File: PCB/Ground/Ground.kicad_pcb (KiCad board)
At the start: 2 copper layers, 100 x 86.6 mm, 40 parts, among them J1 Conn_01x05_Female, U1 HT16K33-28SOP

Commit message: [update] Groundのネットリストを作成 #4
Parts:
- removed D10, D11, D12, D13, D14, D15, D16, D17, D18, D19, D20, D21, D22, D23, D24, D4, D5, D6, D7, D8, D9: LED, extsui:LED_1608_HandSolderingCustom
- removed D26: D, extsui:LED_1608_HandSolderingCustom
- removed J1: Conn_01x05_Female, Connector_PinHeader_2.54mm:PinHeader_1x05_P2.54mm_Vertical
- added C2: 0.1uF, extsui:C_1608_HandSolderingCustom, F.Cu at (115.0, 86.5)
- added C3: 22pF, extsui:C_1608_HandSolderingCustom, F.Cu at (144.5, 84.0)
- added C4: 22pF, extsui:C_1608_HandSolderingCustom, F.Cu at (144.5, 80.0)
- added C5: 10uF, extsui:C_1608_HandSolderingCustom, F.Cu at (115.2, 76.5)
- added C6: 0.1u, extsui:C_1608_HandSolderingCustom, F.Cu at (134.2, 88.5)
- added C7: 0.1u, extsui:C_1608_HandSolderingCustom, F.Cu at (124.3, 76.5)
- added C8: 0.1u, extsui:C_1608_HandSolderingCustom, F.Cu at (135.2, 76.5)
- added CN1: GROVE, OPL_Connector:HW4-2.0-90D, F.Cu at (130.0, 67.5)
- added CN2: GROVE, OPL_Connector:HW4-2.0-90D, F.Cu at (97.5, 85.0)
- added CN3: GROVE, OPL_Connector:HW4-2.0-90D, F.Cu at (97.5, 125.0)
- added CN4: GROVE, OPL_Connector:HW4-2.0-90D, F.Cu at (162.5, 125.0)
- added CN5: GROVE, OPL_Connector:HW4-2.0-90D, F.Cu at (162.5, 85.0)
- added CN6: TTL-232R-3V3, Connector_PinHeader_2.54mm:PinHeader_1x06_P2.54mm_Horizontal, B.Cu at (115.0, 105.0)
- added CN7: ST-LINK, Connector_PinHeader_2.54mm:PinHeader_1x06_P2.54mm_Horizontal, B.Cu at (157.5, 105.0)
- added CN8: Conn_01x05_Female, Connector_PinHeader_2.54mm:PinHeader_1x05_P2.54mm_Vertical, F.Cu at (125.0, 92.5)
- added CN9: CardEdgeConnector5P, extsui:CONN_CARD_EDGE_395-010-521-201, F.Cu at (130.0, 105.0)
- added R4: 10k, extsui:C_1608_HandSolderingCustom, F.Cu at (121.5, 114.5)
- added SW1: RESET, Button_Switch_THT:SW_PUSH_6mm_H8mm, F.Cu at (117.5, 137.5)
- added SW2: MODE, Button_Switch_THT:SW_PUSH_6mm_H8mm, F.Cu at (135.0, 137.5)
- added U2: NJM2845DL1-33, Package_TO_SOT_SMD:TO-252-2, F.Cu at (111.0, 81.5)
- added Y1: 8MHz, Crystal:Crystal_HC49-4H_Vertical, F.Cu at (140.0, 84.5)
- C1: value 0.1u -> 47uF; footprint extsui:C_1608_HandSolderingCustom -> Capacitor_THT:CP_Radial_D5.0mm_P2.50mm; moved to F.Cu
- D1, D2: value LED -> SS2040FL; footprint extsui:LED_1608_HandSolderingCustom -> Diode_SMD:D_SOD-123F
- JP1: value A2 -> JP_BOOT; footprint Jumper:SolderJumper-2_P1.3mm_Open_RoundedPad1.0x1.5mm -> Connector_PinHeader_2.54mm:PinHeader_1x02_P2.54mm_Horizontal; moved to F.Cu
- JP2: value A1 -> Jumper_NO_Small; moved to F.Cu
- JP3: value A0 -> Jumper_NO_Small; moved to F.Cu
- R1, R2, R3: value 39k -> 10k; footprint extsui:R_1608_HandSolderingCustom -> extsui:C_1608_HandSolderingCustom; moved to F.Cu
- U1: value HT16K33-28SOP -> STM32F303K8T6; footprint Package_SO:SOIC-28W_7.5x18.7mm_P1.27mm -> Package_QFP:LQFP-32_7x7mm_P0.8mm; moved to F.Cu
- moved D3 55.9 mm to (145.3, 91.0), turned to 180 degrees
- moved JP1 50.8 mm to (117.5, 72.5), turned to 90 degrees
- moved C1 49.0 mm to (140.0, 70.0)
- moved R1 46.7 mm to (120.2, 76.5), turned to 0 degrees
- moved R2 42.5 mm to (141.2, 91.0), turned to 0 degrees
- moved D2 40.0 mm to (119.5, 81.5), turned to 90 degrees
- moved U1 38.5 mm to (130.0, 82.5), turned to 180 degrees
- moved D1 14.4 mm to (110.0, 98.5), turned to 270 degrees
- moved R3 10.9 mm to (121.5, 117.0), turned to 0 degrees
- moved JP2 3.95 mm to (115.8, 117.0), turned to 180 degrees
- moved JP3 3.95 mm to (115.8, 114.5), turned to 180 degrees
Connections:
- C1 pad 1: +5V -> 5V
- D1 pad 1: Net-(D1-Pad1) -> 5V
- D1 pad 2: Net-(D1-Pad2) -> Net-(CN6-Pad3)
- D2 pad 1: Net-(D1-Pad1) -> 5V
- D2 pad 2: Net-(D18-Pad2) -> 3V3
- D3 pad 1: Net-(D1-Pad1) -> GND
- D3 pad 2: Net-(D19-Pad2) -> Net-(D3-Pad2)
- JP1 pad 1: Net-(JP1-Pad1) -> 3V3
- JP1 pad 2: Net-(D1-Pad2) -> Net-(JP1-Pad2)
- JP2 pad 2: Net-(D18-Pad2) -> LOWER_SCL
- JP3 pad 2: Net-(D19-Pad2) -> LOWER_SDA
- R1 pad 1: Net-(JP1-Pad1) -> Net-(JP1-Pad2)
- R1 pad 2: Net-(D26-Pad1) -> GND
- R2 pad 1: Net-(JP2-Pad1) -> Net-(R2-Pad1)
- R2 pad 2: Net-(D26-Pad1) -> Net-(D3-Pad2)
- R3 pad 1: Net-(JP3-Pad1) -> 3V3
- R3 pad 2: Net-(D26-Pad1) -> Net-(JP2-Pad1)
- U1 pad 1: GND -> 3V3
- U1 pad 12: Net-(D14-Pad2) -> LOWER_SCL
- U1 pad 13: Net-(D13-Pad2) -> LOWER_SDA
- U1 pad 16: Net-(D10-Pad2) -> GND
- U1 pad 17: Net-(D9-Pad2) -> 3V3
- U1 pad 19: Net-(D23-Pad2) -> Net-(R2-Pad1)
- U1 pad 2: Net-(D1-Pad1) -> Net-(C3-Pad1)
- U1 pad 23: Net-(D19-Pad2) -> SWDIO
- U1 pad 24: Net-(D18-Pad2) -> SWCLK
- U1 pad 25: Net-(D1-Pad2) -> TXD
- U1 pad 26: SCL -> SWO
- U1 pad 27: SDA -> Net-(U1-Pad27)
- U1 pad 28: +5V -> Net-(U1-Pad28)
- U1 pad 4: Net-(U1-Pad4) -> NRST
- U1 pad 5: Net-(U1-Pad5) -> 3V3
- U1 pad 8: Net-(U1-Pad8) -> RXD
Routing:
- net Net-(D1-Pad1): track 251.6 -> 0.00 mm, vias 15 -> 0
- net Net-(C4-Pad1): track 170.1 -> 0.00 mm, vias 8 -> 0
- net Net-(D13-Pad2): track 27.1 -> 0.00 mm, vias 1 -> 0
- net Net-(D14-Pad2): track 27.0 -> 0.00 mm, vias 1 -> 0
- net Net-(U1-Pad14): track 26.3 -> 0.00 mm, vias 1 -> 0
- net Net-(U1-Pad11): track 26.0 -> 0.00 mm, vias 1 -> 0
- net Net-(SW2-Pad1): track 23.3 -> 0.00 mm, vias 1 -> 0
- net Net-(U1-Pad15): track 22.0 -> 0.00 mm, vias 1 -> 0
- net Net-(D23-Pad2): track 21.7 -> 0.00 mm, vias 1 -> 0
- net Net-(D10-Pad2): track 21.3 -> 0.00 mm, vias 1 -> 0
- net Net-(D1-Pad2): track 19.6 -> 0.00 mm, vias 1 -> 0
- net Net-(U1-Pad21): track 17.9 -> 0.00 mm, vias 1 -> 0
- net Net-(U1-Pad22): track 16.6 -> 0.00 mm, vias 1 -> 0
- net Net-(D18-Pad2): track 15.5 -> 0.00 mm, vias 1 -> 0
- net Net-(D19-Pad2): track 14.4 -> 0.00 mm, vias 1 -> 0
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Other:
- outline, holes or cut-outs redrawn
- board text added: "@ext_sui 2020.05"
- board text added: "Ground Growing v1.0"
- board text removed: "@ext_sui 2020.04"
- board text removed: "Tile Growing v1.0"

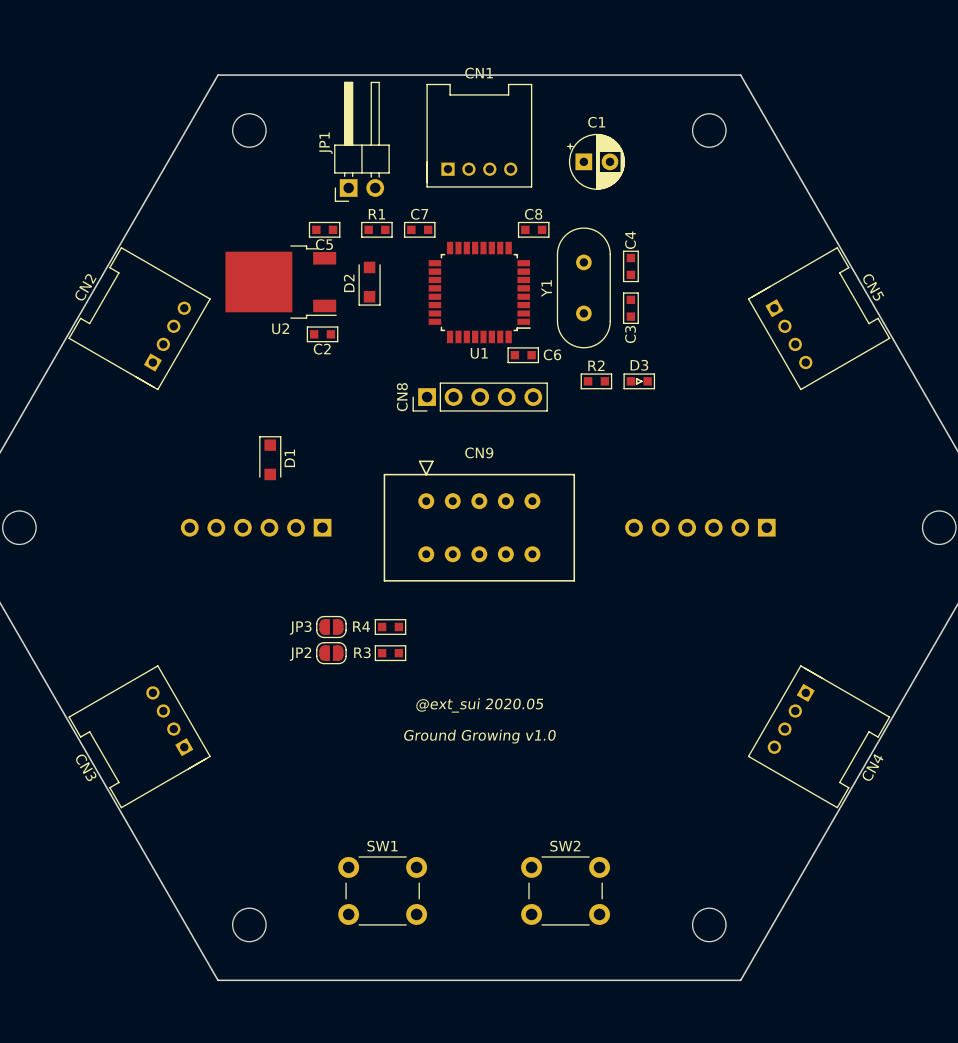
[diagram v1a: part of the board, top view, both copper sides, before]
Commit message: [update] Groundの部品配置のベース作成 #4
* 電解コンデンサC1のシルク幅を5.0mmから6.3mmのものに変更
* GROVEコネクタの位置を厳密な線分の中心に移動
* 小物・シルク等を調整
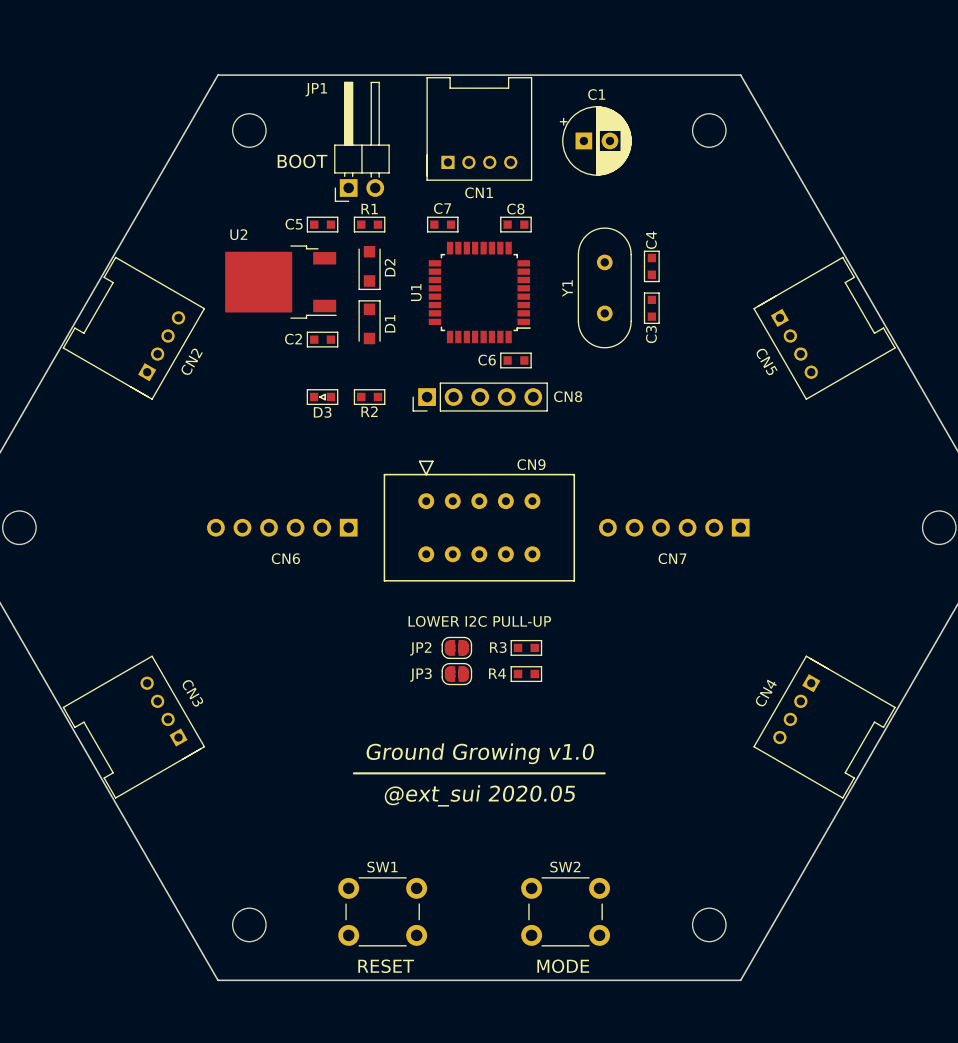
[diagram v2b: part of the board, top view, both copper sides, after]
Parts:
- C1: footprint Capacitor_THT:CP_Radial_D5.0mm_P2.50mm -> Capacitor_THT:CP_Radial_D6.3mm_P2.50mm
- moved D3 30.3 mm to (115.0, 92.5), turned to 0 degrees
- moved R2 21.8 mm to (119.5, 92.5), turned to 180 degrees
- moved D1 16.1 mm to (119.5, 85.5)
- moved R4 13.8 mm to (134.5, 119.0)
- moved R3 13.0 mm to (134.5, 116.5)
- moved JP3 12.8 mm to (127.8, 119.0)
- moved JP2 12.0 mm to (127.8, 116.5)
- moved CN6 2.50 mm to (117.5, 105.0)
- moved CN7 2.50 mm to (155.0, 105.0)
- moved C7 2.26 mm to (126.5, 76.0), turned to 180 degrees
- moved C1 2.00 mm to (140.0, 68.0)
- moved C3 2.00 mm to (146.5, 84.0)
- moved C4 2.00 mm to (146.5, 80.0)
- moved SW1 2.00 mm to (117.5, 139.5)
- moved SW2 2.00 mm to (135.0, 139.5)
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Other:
- board text added: "+5V"
- board text added: "3V3"
- board text added: "BOOT"
- board text added: "CTS"
- board text added: "GND"
- board text added: "LOWER I2C PULL-UP"
- board text added: "MODE"
- board text added: "NRST"
- board text added: "RESET"
- board text added: "RTS"
- board text added: "RXD"
- board text added: "ST-LINK"
- board text added: "SWCLK"
- board text added: "SWDIO"
- board text added: "SWO"
- board text added: "TTL-232R-3V3"
- board text added: "TXD"

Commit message: [update] Groundの電源周りを配線 #4
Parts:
- turned C4 to 270 degrees
- turned R1 to 180 degrees
- turned R3 to 180 degrees
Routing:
- net 5V: track 0.00 -> 216.4 mm
- net 3V3: track 0.00 -> 38.3 mm
- net Net-(CN6-Pad3): track 0.00 -> 24.0 mm
- net Net-(C3-Pad1): track 0.00 -> 16.1 mm
- net Net-(C4-Pad1): track 0.00 -> 16.0 mm
- net Net-(JP3-Pad1): track 0.00 -> 5.20 mm
- net Net-(JP2-Pad1): track 0.00 -> 5.20 mm
- net Net-(CN9-Pad4): track 0.00 -> 5.08 mm
- net LOWER_SDA: track 0.00 -> 5.08 mm
- net LOWER_SCL: track 0.00 -> 5.08 mm
- net GND: track 0.00 -> 5.08 mm

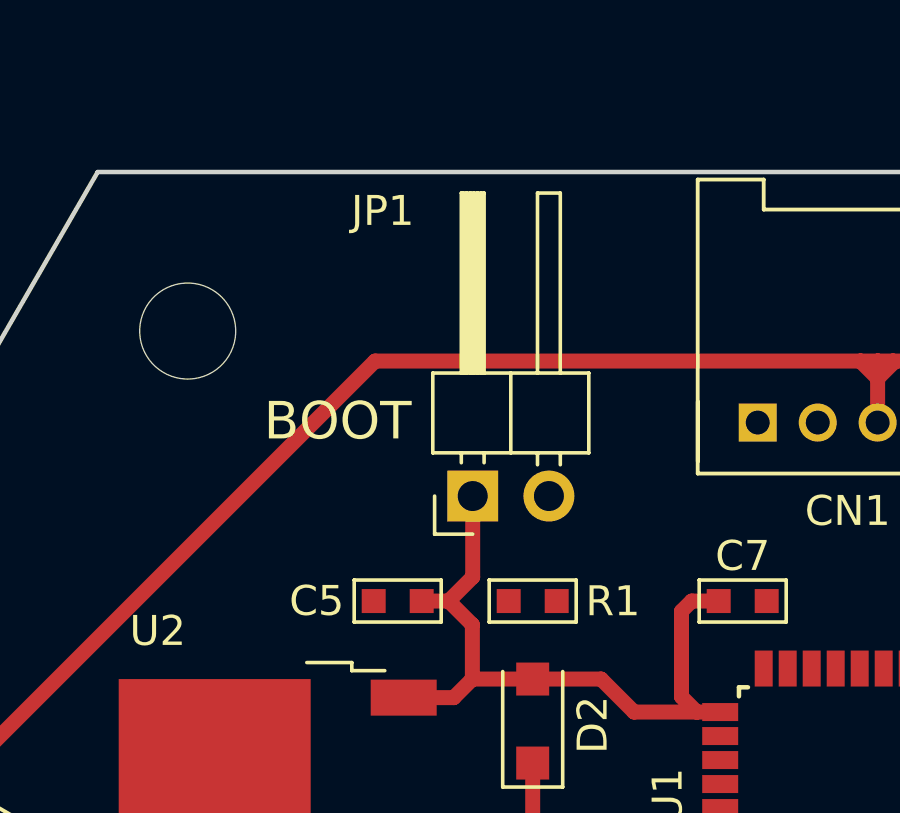
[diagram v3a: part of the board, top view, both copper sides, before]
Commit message: [update] Groundの配線でCard部のベタ禁止領域を追加 #4
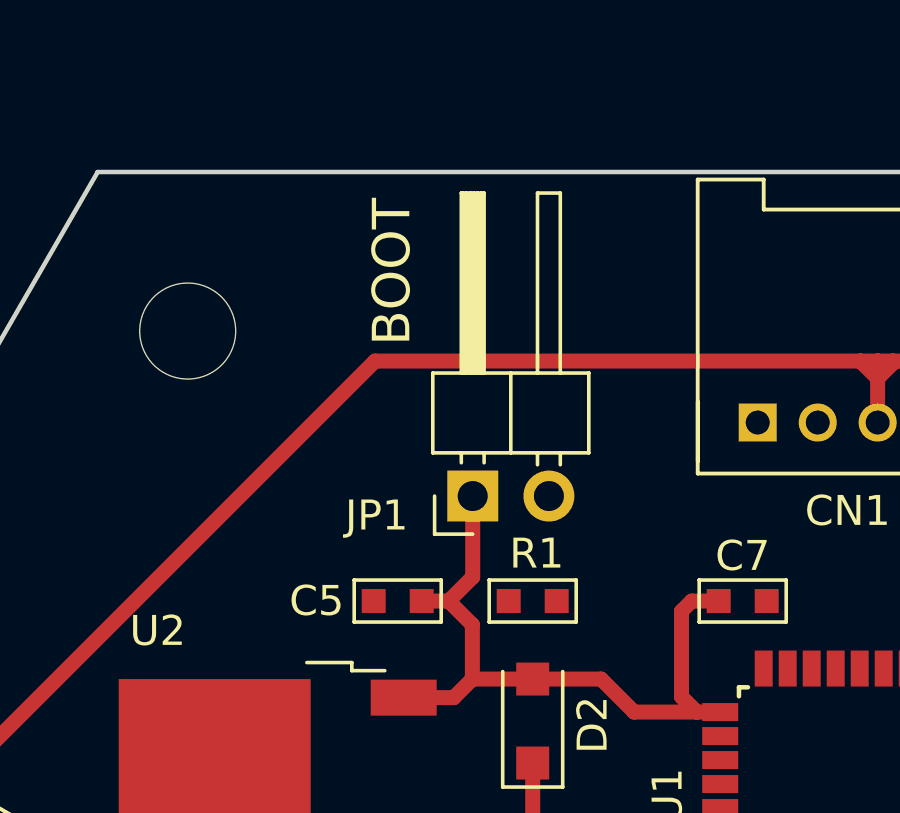
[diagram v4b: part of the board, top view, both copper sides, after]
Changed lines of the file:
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@@
   )
   (setup
-    (last_trace_width 0.5)
+    (last_trace_width 0.25)
     (user_trace_width 0.5)
     (user_trace_width 1)
@@
     (tags "resistor 0603")
     (attr smd)
-    (fp_text reference R1 (at -2.674 -0.0095 180) (layer F.SilkS)
+    (fp_text reference R1 (at -0.134 1.578 180) (layer F.SilkS)
       (effects (font (size 1 1) (thickness 0.15)))
     )
@@
     (descr "Through hole angled pin header, 1x02, 2.54mm pitch, 6mm pin length, single row")
     (tags "Through hole angled pin header THT 1x02 2.54mm single row")
-    (fp_text reference JP1 (at 9.5 -3) (layer F.SilkS)
+    (fp_text reference JP1 (at -0.652 -3.2) (layer F.SilkS)
       (effects (font (size 1 1) (thickness 0.15)))
     )
@@
   )
   (gr_line (start 118 128.5) (end 142 128.5) (layer F.SilkS) (width 0.2))
-  (gr_text BOOT (at 113 70) (layer F.SilkS)
+  (gr_text BOOT (at 114.808 65.024 90) (layer F.SilkS)
     (effects (font (size 1.25 1.25) (thickness 0.2)))
   )
@@
       )
     )
+  )
+  (zone (net 0) (net_name "") (layer F.Cu) (hatch edge 0.508)
+    (connect_pads (clearance 0.508))
+    (min_thickness 0.254)
+    (keepout (tracks allowed) (vias allowed) (copperpour not_allowed))
+    (fill (arc_segments 16) (thermal_gap 0.508) (thermal_bridge_width 0.508))
+    (polygon
+      (pts
+        (xy 136.144 107.696) (xy 136.144 102.362) (xy 133.604 102.362) (xy 133.604 107.696)
+      )
+    )

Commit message: [update] Groundの配線への回路図反映と電解コンデンサ位置修正
* 電解コンデンサC1を左に移動することでCN5の+5Vラインを
  中央から配線できるように修正した。
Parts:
- added JP4: Jumper_NO_Small, Jumper:SolderJumper-2_P1.3mm_Open_RoundedPad1.0x1.5mm, F.Cu at (146.7, 92.4)
- moved JP3 31.2 mm to (144.2, 92.4), turned to 90 degrees
- moved JP2 27.8 mm to (141.7, 92.4), turned to 90 degrees
- moved JP1 23.0 mm to (140.5, 72.5)
- moved C1 21.5 mm to (118.5, 68.5), turned to 90 degrees
- moved R3 4.00 mm to (130.5, 116.5)
- moved R4 4.00 mm to (130.5, 119.0)
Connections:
- JP2 pad 1: Net-(JP2-Pad1) -> GND
- JP2 pad 2: LOWER_SCL -> Net-(JP2-Pad2)
- JP3 pad 1: Net-(JP3-Pad1) -> GND
- JP3 pad 2: LOWER_SDA -> Net-(JP3-Pad2)
- R3 pad 2: Net-(JP2-Pad1) -> LOWER_SCL
- R4 pad 2: Net-(JP3-Pad1) -> LOWER_SDA
- U1 pad 10: Net-(U1-Pad10) -> Net-(JP3-Pad2)
- U1 pad 9: Net-(U1-Pad9) -> Net-(JP2-Pad2)
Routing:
- net LOWER_SDA: track 5.08 -> 159.1 mm, vias 0 -> 2
- net LOWER_SCL: track 5.08 -> 158.5 mm, vias 0 -> 2
- net UPPER_SCL: track 0.00 -> 18.1 mm, vias 0 -> 1
- net UPPER_SDA: track 0.00 -> 18.1 mm, vias 0 -> 1
- net GND: track 5.08 -> 15.1 mm
- net 5V: track 216.4 -> 210.6 mm, vias 0 -> 1
- net Net-(JP3-Pad1): track 5.20 -> 0.00 mm
- net Net-(JP2-Pad1): track 5.20 -> 0.00 mm
- net 3V3: track 38.3 -> 34.4 mm

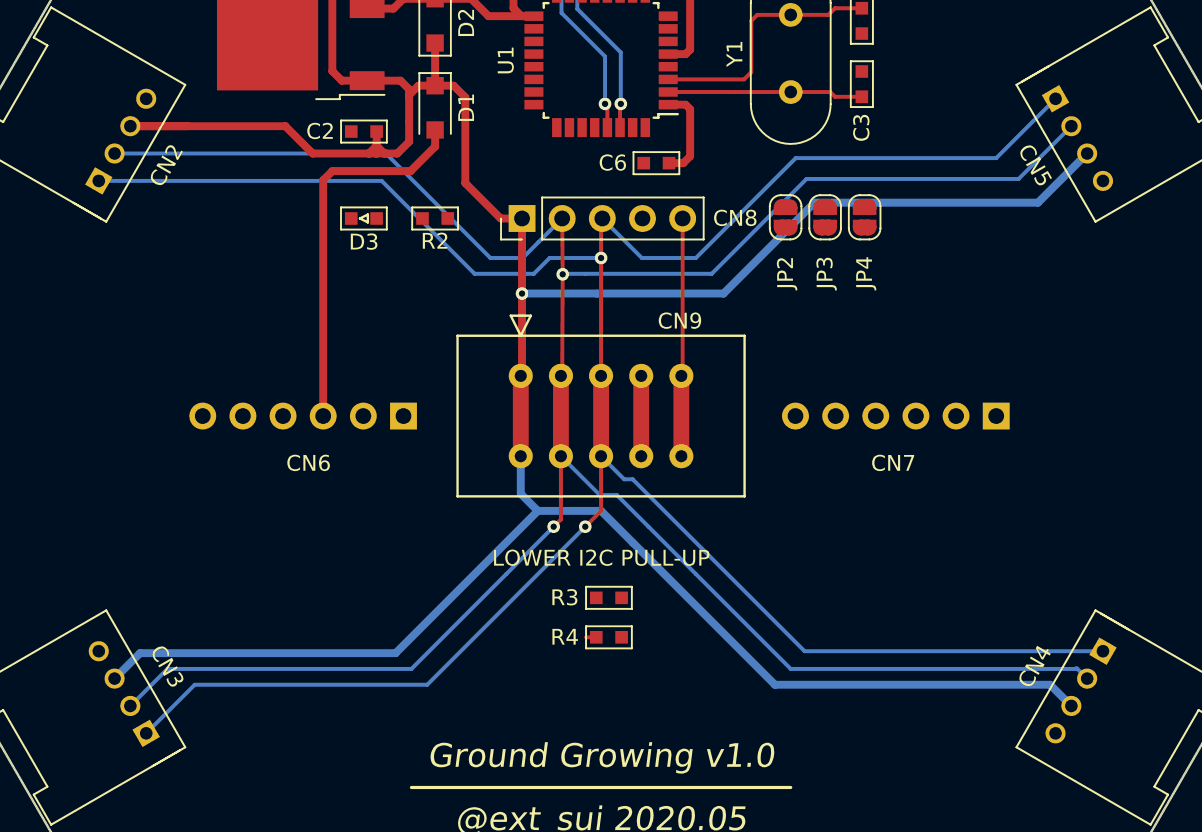
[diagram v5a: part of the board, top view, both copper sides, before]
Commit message: [update] Groundの回路図のCN2-5のI2Cバス配線を改善 #4
* CN2-5のI2Cバス配線を点対称になるように修正
  ※コネクタ位置が逆順になるため線対称にすることは不可能
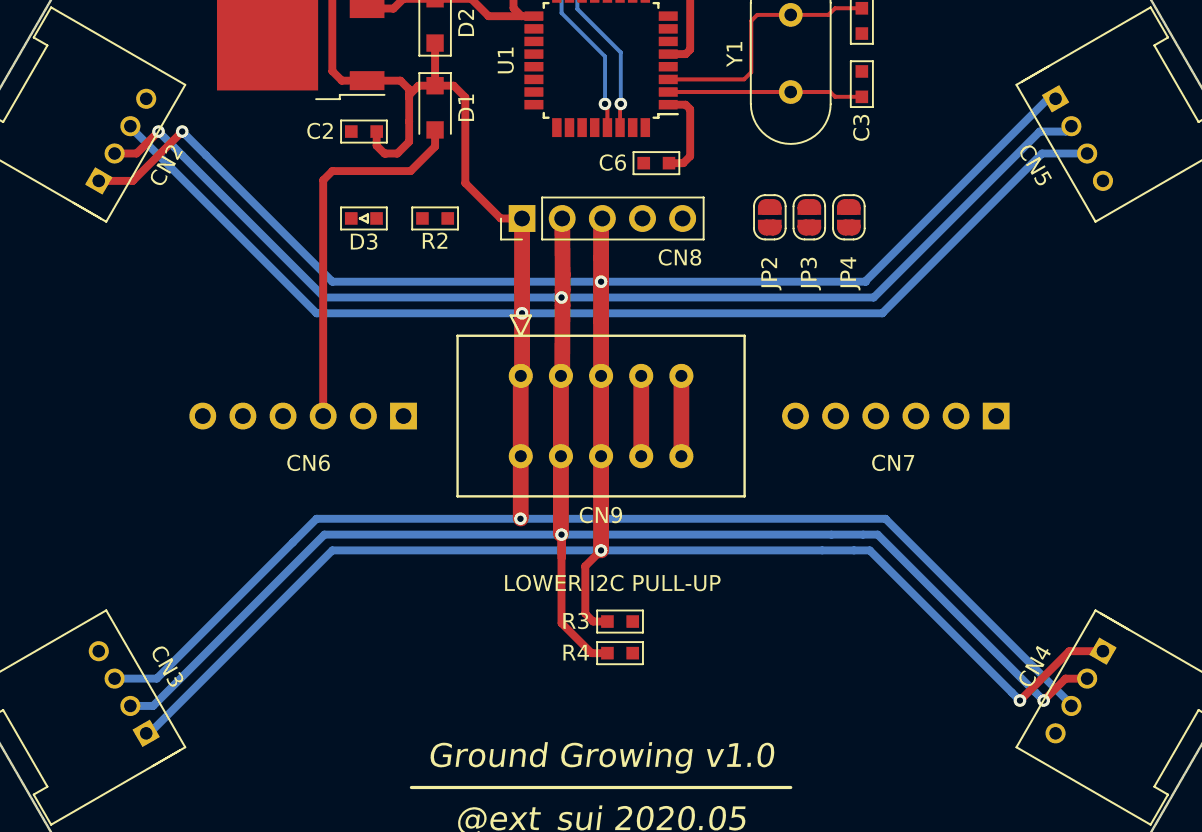
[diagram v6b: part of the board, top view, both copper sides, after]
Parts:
- moved R3 1.66 mm to (131.2, 118.0)
- moved R4 1.22 mm to (131.2, 120.0)
- moved JP2 1.00 mm to (140.7, 92.4)
- moved JP3 1.00 mm to (143.2, 92.4)
- moved JP4 1.00 mm to (145.7, 92.4)
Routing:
- net LOWER_SDA: track 159.1 -> 170.9 mm, vias 2 -> 4
- net LOWER_SCL: track 158.5 -> 168.7 mm, vias 2 -> 4
- net GND: track 15.1 -> 5.19 mm
- net 5V: track 210.6 -> 219.4 mm, vias 1 -> 2
